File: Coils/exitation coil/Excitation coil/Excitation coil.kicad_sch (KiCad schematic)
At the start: 6 parts, among them J1 Conn_01x02_Socket, J2 Conn_01x02_Pin

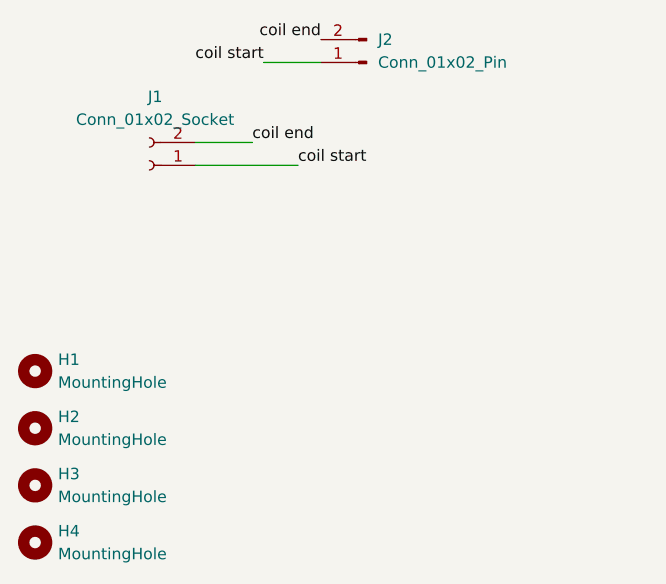
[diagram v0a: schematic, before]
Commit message: added 3d models for OPA3692, THS3091 and BNC connector
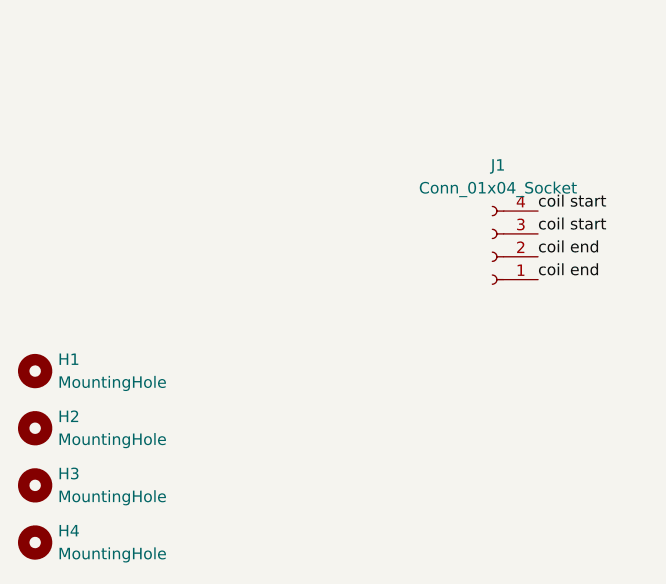
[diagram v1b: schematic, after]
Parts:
- removed J1: Conn_01x02_Socket, Connector_PinSocket_2.54mm:PinSocket_1x02_P2.54mm_Vertical, symbol Connector:Conn_01x02_Socket
- removed J2: Conn_01x02_Pin, Connector_PinHeader_2.54mm:PinHeader_1x02_P2.54mm_Vertical, symbol Connector:Conn_01x02_Pin
- added J1: Conn_01x04_Socket, Connector_PinSocket_2.54mm:PinSocket_1x04_P2.54mm_Horizontal, symbol Connector:Conn_01x04_Socket
- H1, H2, H3, H4: footprint MountingHole:MountingHole_5mm_Pad -> MountingHole:MountingHole_3.2mm_M3_Pad
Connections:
- net coil end: now also J1.1 (Pin_1), J1.2 (Pin_2)
- net coil start: now also J1.3 (Pin_3), J1.4 (Pin_4)

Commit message: Added via stiching to TX board, moved almost all vias off of pads, increased the trace width for the power supply and changed coil connector to horizontal socket
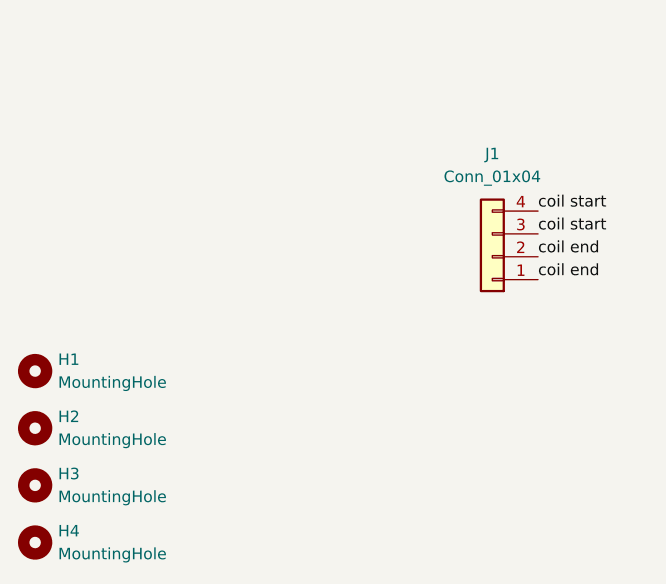
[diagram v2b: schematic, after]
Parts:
- removed J1: Conn_01x04_Socket, Connector_PinSocket_2.54mm:PinSocket_1x04_P2.54mm_Horizontal, symbol Connector:Conn_01x04_Socket
- added J1: Conn_01x04, Connector_PinHeader_2.54mm:PinHeader_1x04_P2.54mm_Horizontal, symbol Connector_Generic:Conn_01x04
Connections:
- net coil end: now also J1.1 (Pin_1), J1.2 (Pin_2)
- net coil start: now also J1.3 (Pin_3), J1.4 (Pin_4)
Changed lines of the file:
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@@
+	)
+	(symbol
+		(lib_id "Connector_Generic:Conn_01x04")
+		(at 129.54 67.31 180)
+		(unit 1)
+		(exclude_from_sim no)
+		(in_bom yes)
+		(on_board yes)
+		(dnp no)
+		(fields_autoplaced yes)
+		(property "Reference" "J1"
+			(at 129.54 55.88 0)
+			(effects
+				(font
+					(size 1.27 1.27)
+				)
+			)
+		)
+		(property "Value" "Conn_01x04"
+			(at 129.54 58.42 0)
+			(effects
+				(font
+					(size 1.27 1.27)
+				)
+			)
+		)
+		(property "Footprint" "Connector_PinHeader_2.54mm:PinHeader_1x04_P2.54mm_Horizontal"
+			(at 129.54 67.31 0)
+			(effects
+				(font
+					(size 1.27 1.27)
+				)
+				(hide yes)
+			)
+		)
+		(property "Datasheet" "~"
+			(at 129.54 67.31 0)
+			(effects
+				(font
+					(size 1.27 1.27)
+				)
+				(hide yes)
+			)
+		)
+		(property "Description" "Generic connector, single row, 01x04, script generated (kicad-library-utils/schlib/autogen/connector/)"
+			(at 129.54 67.31 0)
+			(effects
+				(font
+					(size 1.27 1.27)
+				)
+				(hide yes)
+			)
+		)
+		(pin "3"
+		)
+		(pin "1"
+		)
+		(pin "2"
+		)
+		(pin "4"
+		)
+		(instances
+			(project "Excitation coil"
+				(path "/fc0e8423-a761-4dc5-b59d-c4f75f80d309"
+					(reference "J1")
+					(unit 1)
+				)
+			)
+		)
 	)
 	(symbol
@@
 					(unit 1)
 				)
-			)
-		)
-	)
-	(symbol
-		(lib_id "Connector:Conn_01x04_Socket")
-		(at 129.54 67.31 180)
-		(unit 1)
-		(exclude_from_sim no)
-		(in_bom yes)
-		(on_board yes)
-		(dnp no)
-		(fields_autoplaced yes)
-		(property "Reference" "J1"
-			(at 130.175 57.15 0)
-			(effects
-				(font
-					(size 1.27 1.27)
-				)
-			)
-		)
-		(property "Value" "Conn_01x04_Socket"
-			(at 130.175 59.69 0)
-			(effects
-				(font
-					(size 1.27 1.27)
-				)
-			)
-		)
-		(property "Footprint" "Connector_PinSocket_2.54mm:PinSocket_1x04_P2.54mm_Horizontal"
-			(at 129.54 67.31 0)
-			(effects
-				(font
-					(size 1.27 1.27)
-				)
-				(hide yes)
-			)
-		)
-		(property "Datasheet" "~"
-			(at 129.54 67.31 0)
-			(effects
-				(font
-					(size 1.27 1.27)
-				)
-				(hide yes)
-			)
-		)
-		(property "Description" "Generic connector, single row, 01x04, script generated"
-			(at 129.54 67.31 0)
-			(effects
-				(font
-					(size 1.27 1.27)
-				)
-				(hide yes)
-			)
-		)
-		(pin "1"
-		)
-		(pin "4"
-		)
-		(pin "2"
-		)
-		(pin "3"
-		)
-		(instances
-			(project "Excitation coil"
-				(path "/fc0e8423-a761-4dc5-b59d-c4f75f80d309"
-					(reference "J1")
-					(unit 1)
-				)
